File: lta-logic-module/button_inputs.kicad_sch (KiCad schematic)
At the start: 27 parts

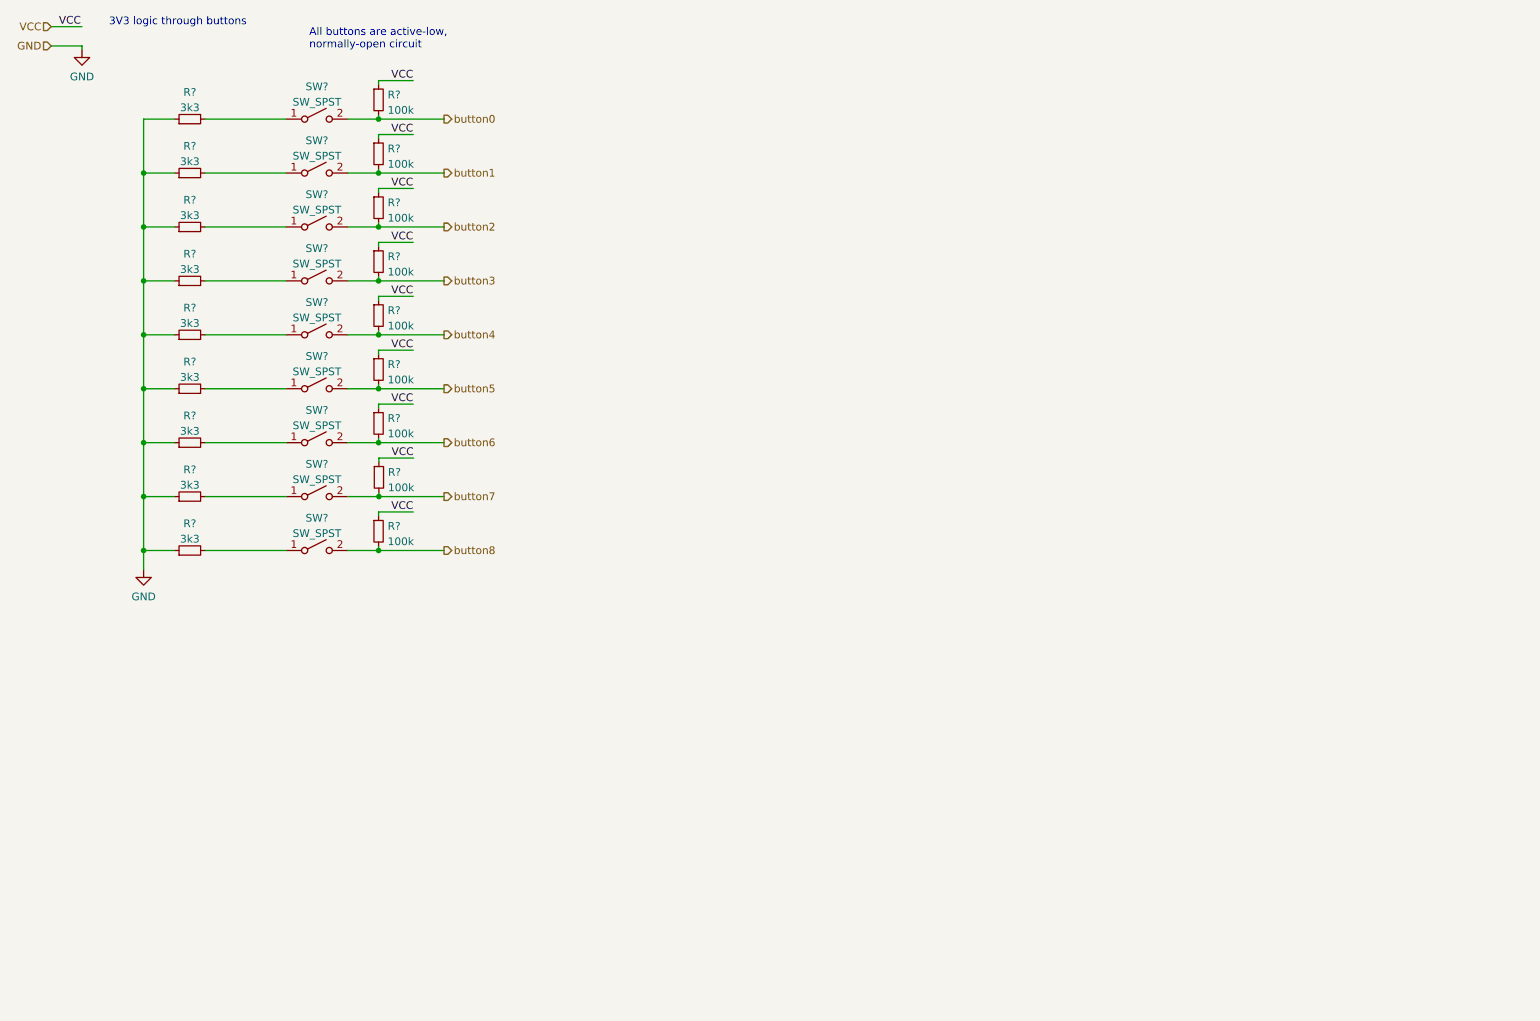
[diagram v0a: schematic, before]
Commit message: Full sketch of logic module schematic.
- Add button inputs
- Add LED signal driver / PWM combination
- Add 5V regulator based on LM2592
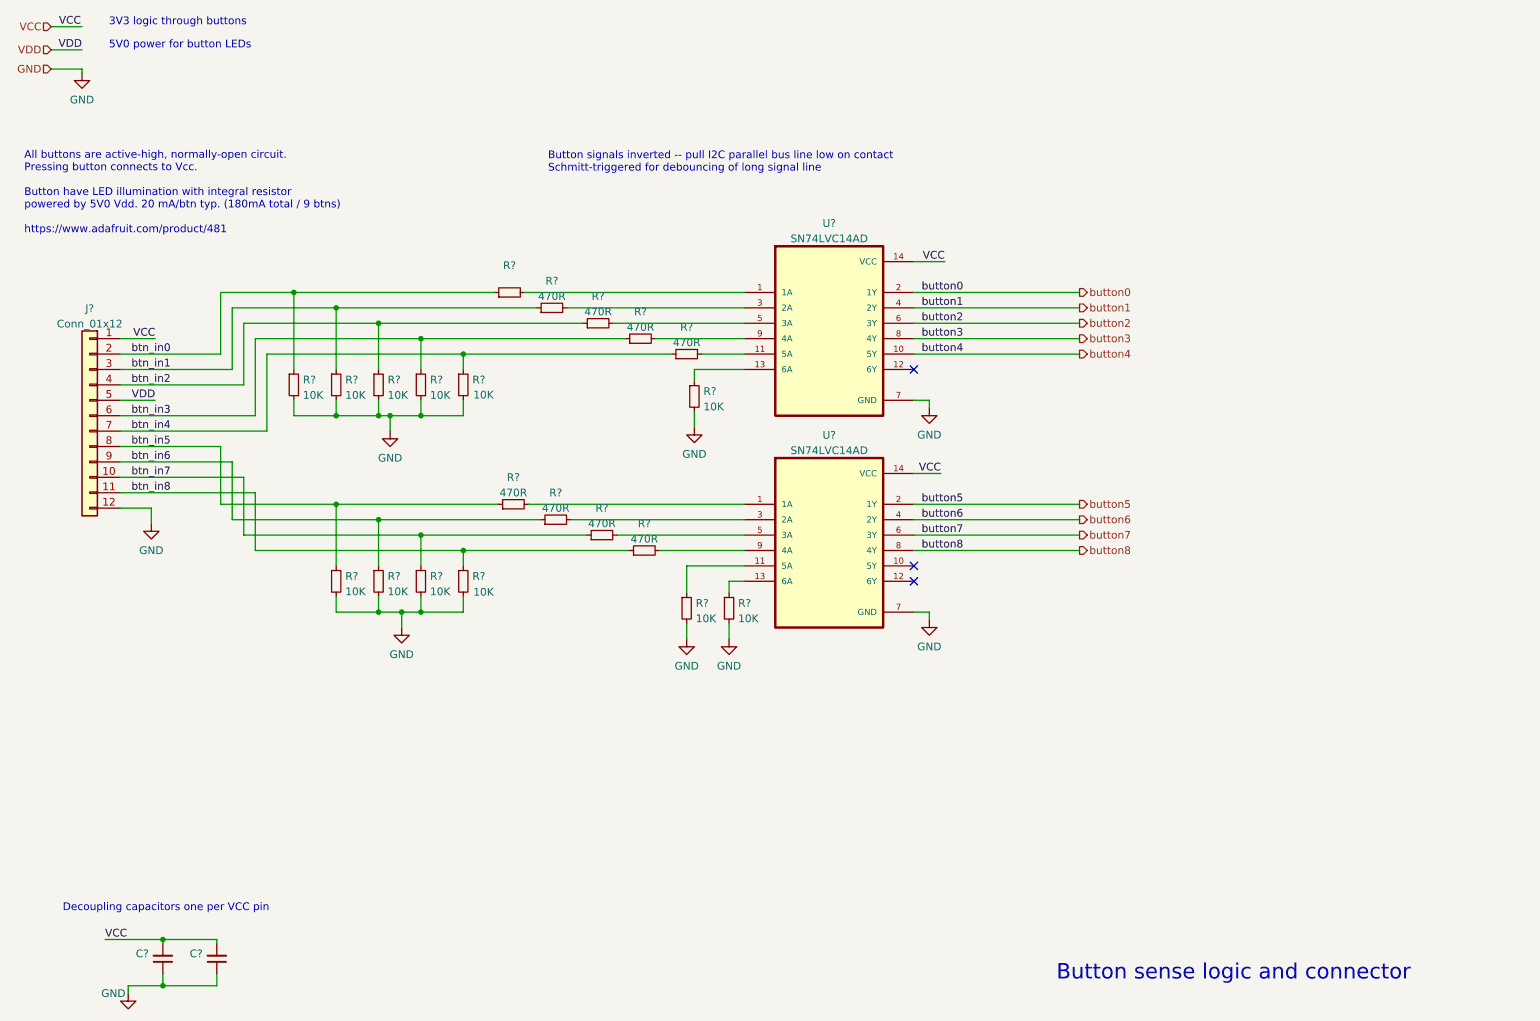
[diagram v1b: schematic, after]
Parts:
- removed R? (x9): 100k, symbol Device:R_Small
- removed R? (x9): 3k3, symbol Device:R_Small
- removed SW? (x9): SW_SPST, symbol Switch:SW_SPST
- added C? (x2): (no value), symbol Device:C_Small
- added J?: Conn_01x12, symbol Connector_Generic:Conn_01x12
- added R? (x8): 470R, symbol Device:R_Small
- added R? (x12): 10K, symbol Device:R_Small
- added R?: (no value), symbol Device:R_Small
- added U? (x2): SN74LVC14AD, Aaron_TI_Parts:TI_SOIC_D_R-PDSO-G14, symbol Aaron-TI-74xx:SN74LVC14AD
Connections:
- net GND: now also C?.1, C?.1, J?.12 (Pin_12), R?.2, R?.2, R?.2, R?.2, R?.2, R?.2, R?.2, R?.2, R?.2, R?.2, R?.2, R?.2, U?.7 (GND), U?.7 (GND)
- net VCC: now also C?.2, C?.2, J?.1 (Pin_1), U?.14 (VCC), U?.14 (VCC)
- net button0: now also U?.2 (1Y)
- net button1: now also U?.4 (2Y)
- net button2: now also U?.6 (3Y)
- net button3: now also U?.8 (4Y)
- net button4: now also U?.10 (5Y)
- net button5: now also U?.2 (1Y)
- net button6: now also U?.4 (2Y)
- net button7: now also U?.6 (3Y)
- net button8: now also U?.8 (4Y)
- new net: R?.2, U?.3 (2A) (x2)
- new net: R?.2, U?.9 (4A) (x2)
- new net: R?.2, U?.5 (3A) (x2)
- new net: R?.2, U?.1 (1A) (x2)
- new net: R?.1, U?.11 (5A)
- new net: R?.1, U?.13 (6A) (x2)
- new net: R?.2, U?.11 (5A)
- new net VDD: J?.5 (Pin_5)
- new net btn_in0: J?.2 (Pin_2), R?.1, R?.1
- new net btn_in1: J?.3 (Pin_3), R?.1, R?.1
- new net btn_in2: J?.4 (Pin_4), R?.1, R?.1
- new net btn_in3: J?.6 (Pin_6), R?.1, R?.1
- new net btn_in4: J?.7 (Pin_7), R?.1, R?.1
- new net btn_in5: J?.8 (Pin_8), R?.1, R?.1
- new net btn_in6: J?.9 (Pin_9), R?.1, R?.1
- new net btn_in7: J?.10 (Pin_10), R?.1, R?.1
- new net btn_in8: J?.11 (Pin_11), R?.1, R?.1
- no-connect marks 0 -> 3
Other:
- note added: "5V0 power for button LEDs"
- note added: "All buttons are active-high, normally-open circuit. Pressing button connects to Vcc. Button have LED illumination with integral resistor powered by 5V0 Vdd. 20 mA/btn typ. (180mA total / 9 btns) https://www.adafruit.com/product/481"
- note added: "Button sense logic and connector"
- note added: "Button signals inverted -- pull I2C parallel bus line low on contact Schmitt-triggered for debouncing of long signal line"
- note added: "Decoupling capacitors one per VCC pin"
- note removed: "All buttons are active-low, normally-open circuit"

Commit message: Fix ERC violations.
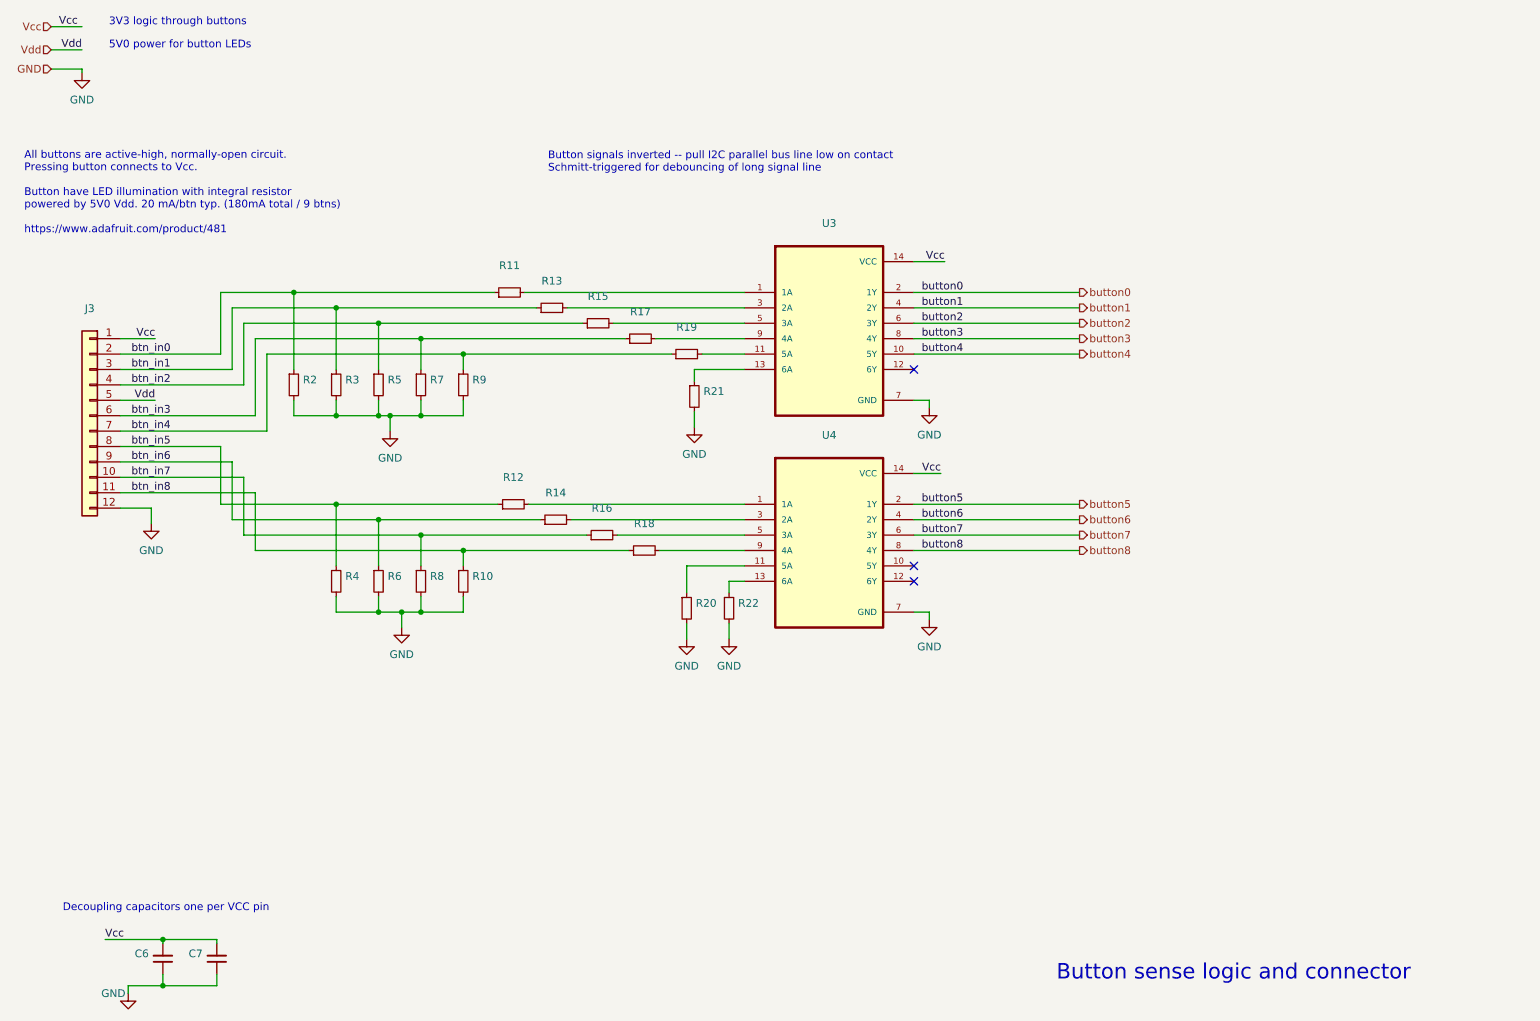
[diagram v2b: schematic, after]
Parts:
- J3: renamed from J?; value Conn_01x12 -> (none)
- R10, R2, R20, R21, R22, R3, R4, R5, R6, R7, R8, R9: renamed from R?; value 10K -> (none)
- R12, R13, R14, R15, R16, R17, R18, R19: renamed from R?; value 470R -> (none)
- U3, U4: renamed from U?; value SN74LVC14AD -> (none); footprint Aaron_TI_Parts:TI_SOIC_D_R-PDSO-G14 -> (none)
- gave numbers to parts that had none: 3
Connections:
- net VCC renamed Vcc
- net VDD renamed Vdd

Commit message: Add TODOs, update some footprints.
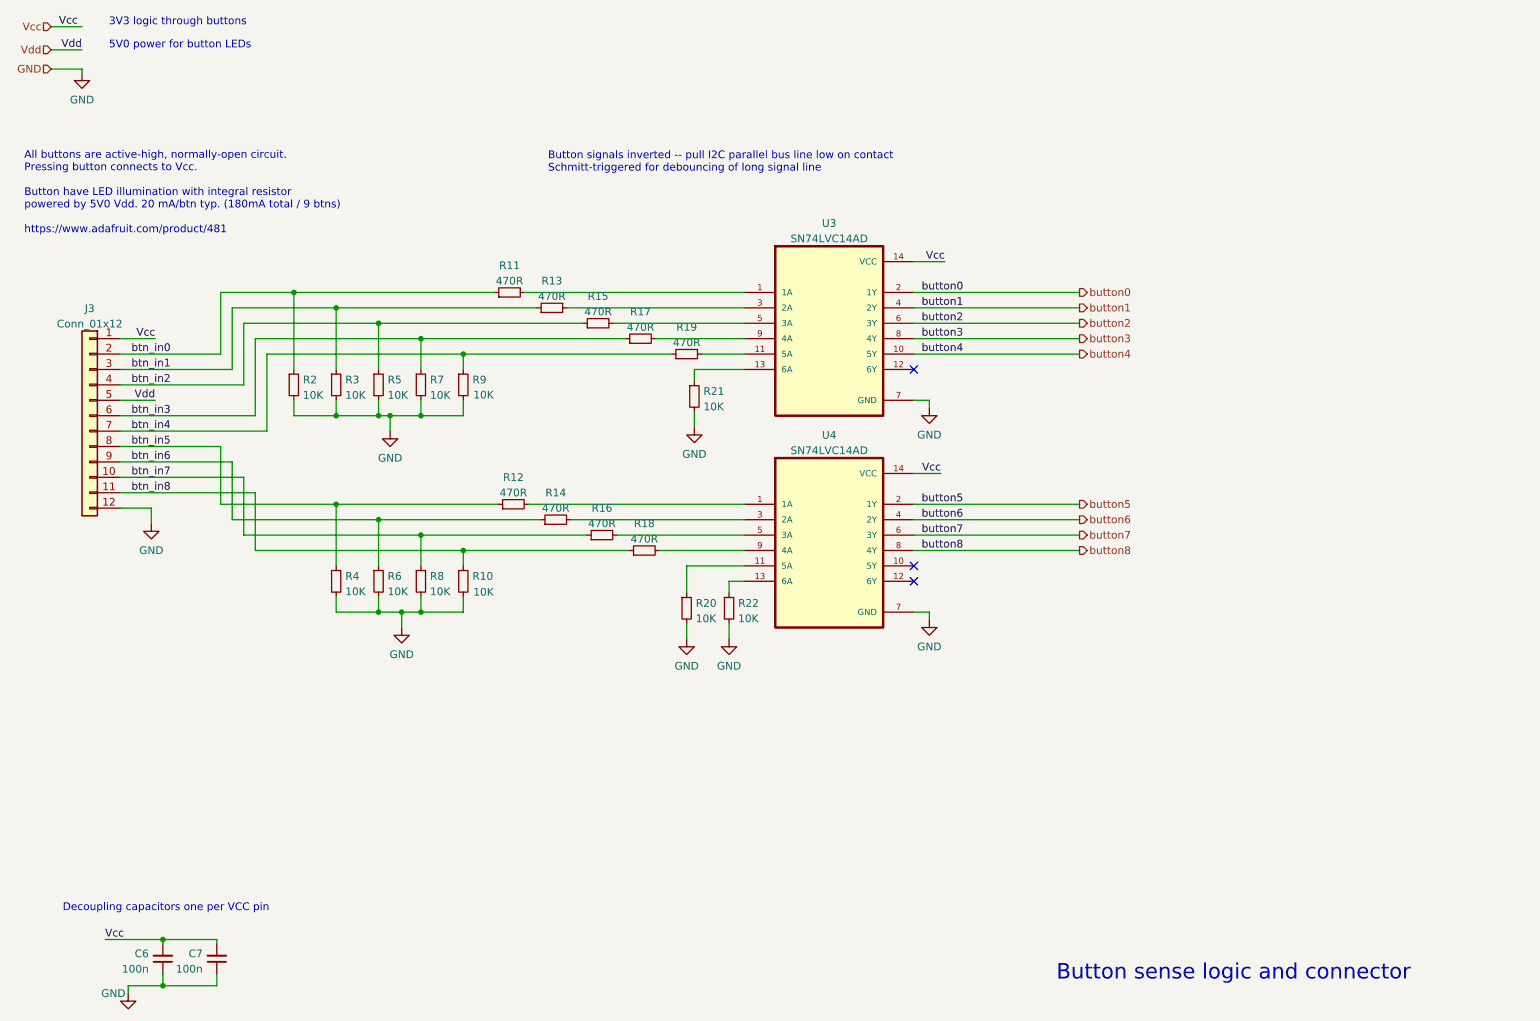
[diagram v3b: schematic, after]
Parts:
- C6, C7: value (none) -> 100n; footprint (none) -> Capacitor_SMD:C_0603_1608Metric; Comment (none) -> 100nF 5% 6.3V 0603 X7R ceramic; 20mOhm < ESR < 10 Ohm; MANUFACTURER (none) -> KYOCERA; MPN (none) -> 06036C104JAT2A
- J3: value (none) -> Conn_01x12; footprint (none) -> Connector_PinHeader_2.54mm:PinHeader_1x12_P2.54mm_Vertical; Comment (none) -> TODO REPLACE FOOTPRINT; MPN (none) -> XXX TODO FIND
- R10, R2, R20, R21, R22, R3, R4, R5, R6, R7, R8, R9: value (none) -> 10K; footprint (none) -> Resistor_SMD:R_0603_1608Metric; Comment (none) -> 10K 0603 resistor; +/-1%; 1/10W; MANUFACTURER (none) -> YAEGO; MPN (none) -> RC0603FR-0710KL
- R11, R12, R13, R14, R15, R16, R17, R18, R19: value (none) -> 470R; footprint (none) -> Resistor_SMD:R_0603_1608Metric; Comment (none) -> 470R 0603 resistor; +/-1%; 1/10W; MANUFACTURER (none) -> YAEGO; MPN (none) -> RC0603FR-07470RL
- U3, U4: value (none) -> SN74LVC14AD; footprint (none) -> Aaron_TI_Parts:TI_SOIC_D_R-PDSO-G14; MANUFACTURER (none) -> Texas Instruments; MPN (none) -> SN74LVC14AD

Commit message: Initial PCB setup
* Configure Elecrow DRC checks for lta-logic-module.
* Switch SN74LVC244A from 'N' PDIP to 'DWR' SOIC footprint.
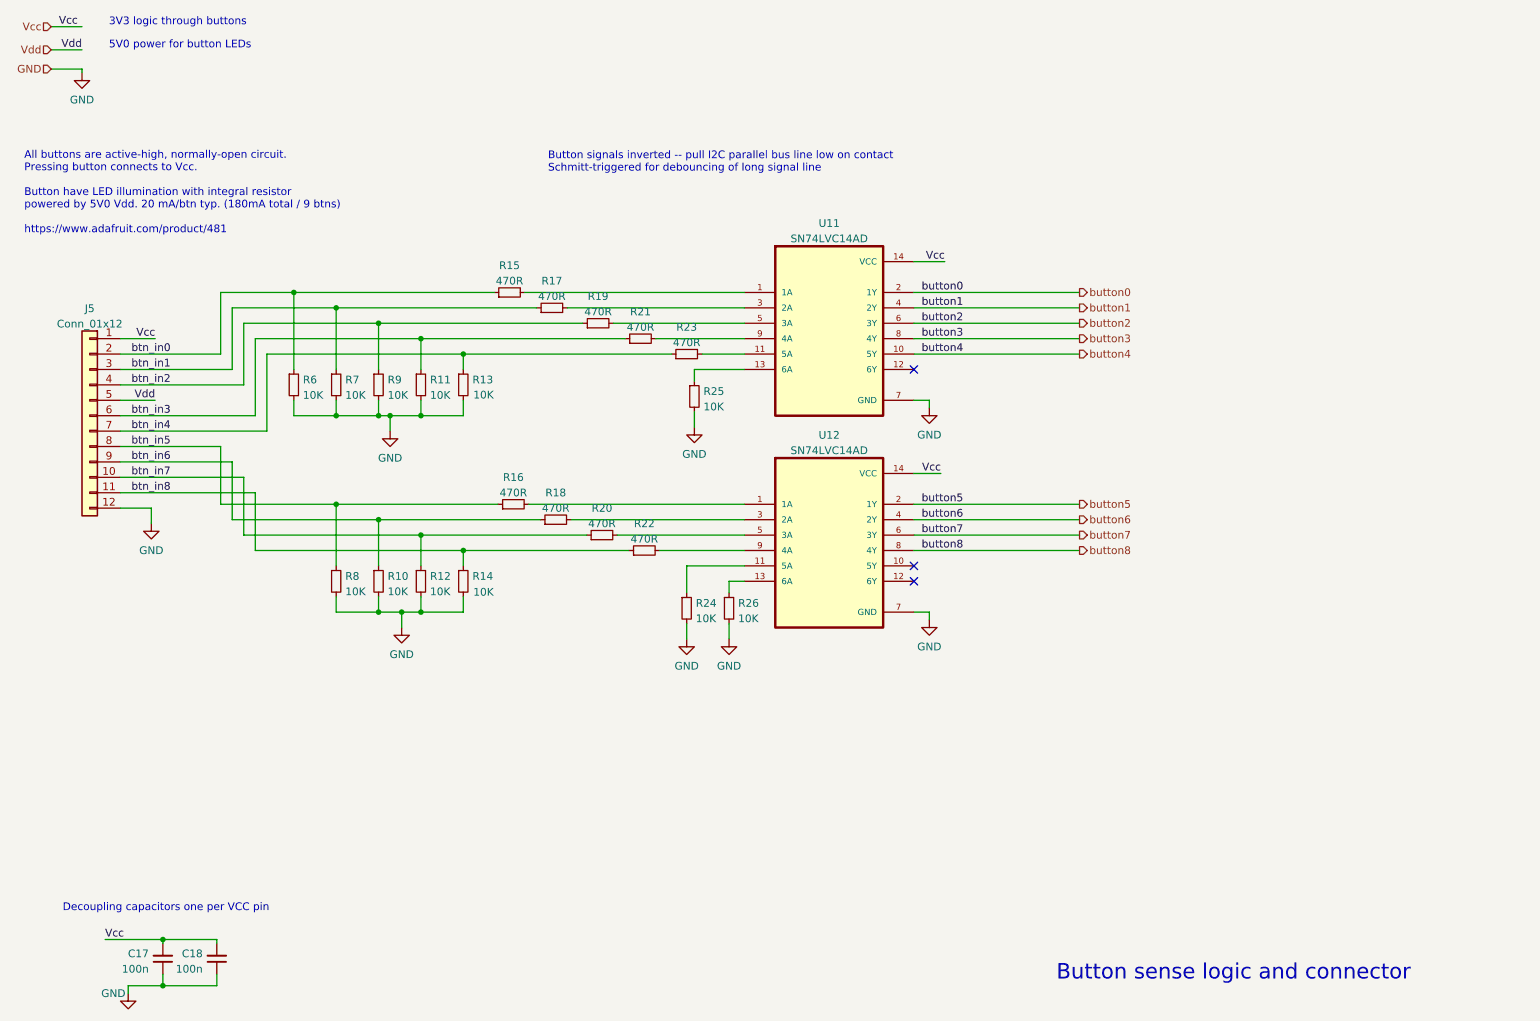
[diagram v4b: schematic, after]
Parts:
- renumbered C6 to C17, C7 to C18, J3 to J5, R6 to R10, R7 to R11, R8 to R12, R9 to R13, R10 to R14, R11 to R15, R12 to R16, R13 to R17, R14 to R18, R15 to R19, R16 to R20, R17 to R21, R18 to R22, R19 to R23, R20 to R24, R21 to R25, R22 to R26, R2 to R6, R3 to R7, R4 to R8, R5 to R9, U3 to U11, U4 to U12
